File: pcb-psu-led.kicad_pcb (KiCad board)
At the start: 2 copper layers, 140 x 80 mm, 16 parts, among them J1 MKDS 1,5/2-5,08, J2 LED PANEL OUT, T1 Talema 70000K, U1 LM78L05ACZ

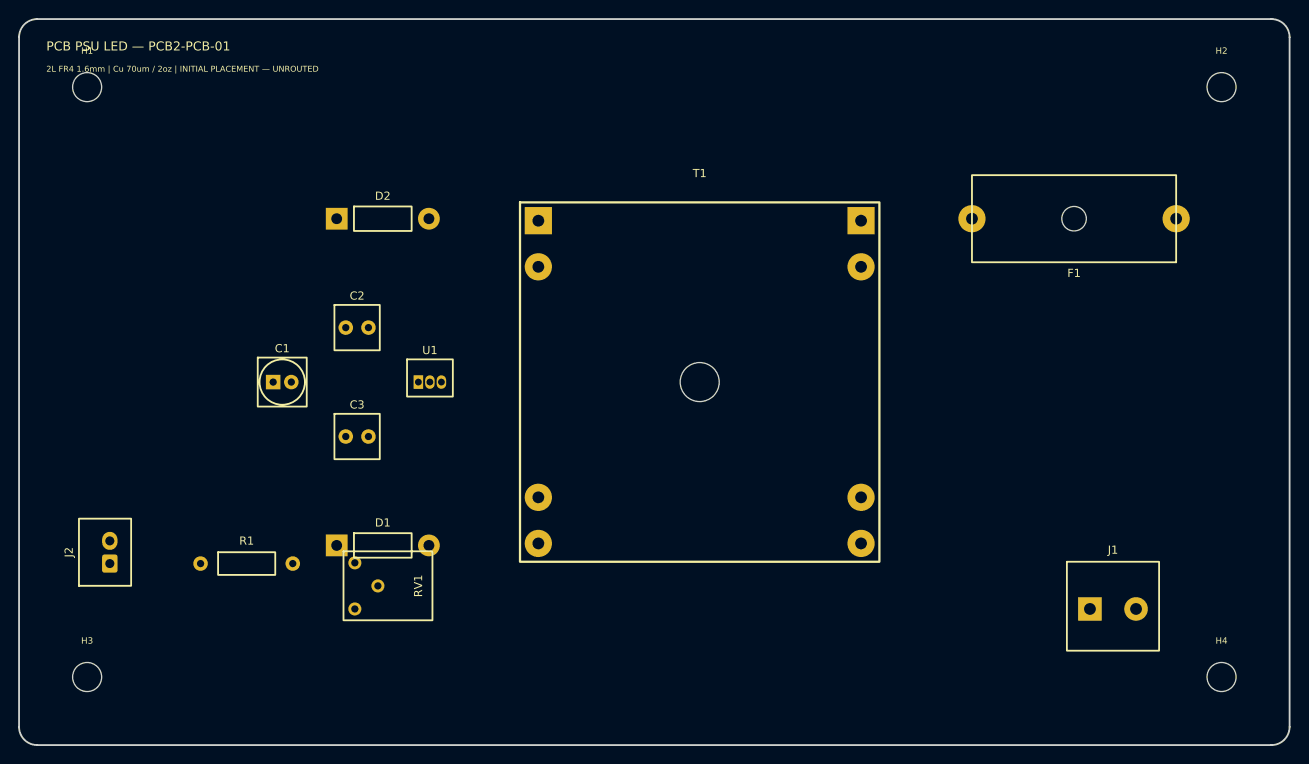
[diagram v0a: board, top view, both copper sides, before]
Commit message: PCB2-PCB-03: route board and segregate mains from SELV
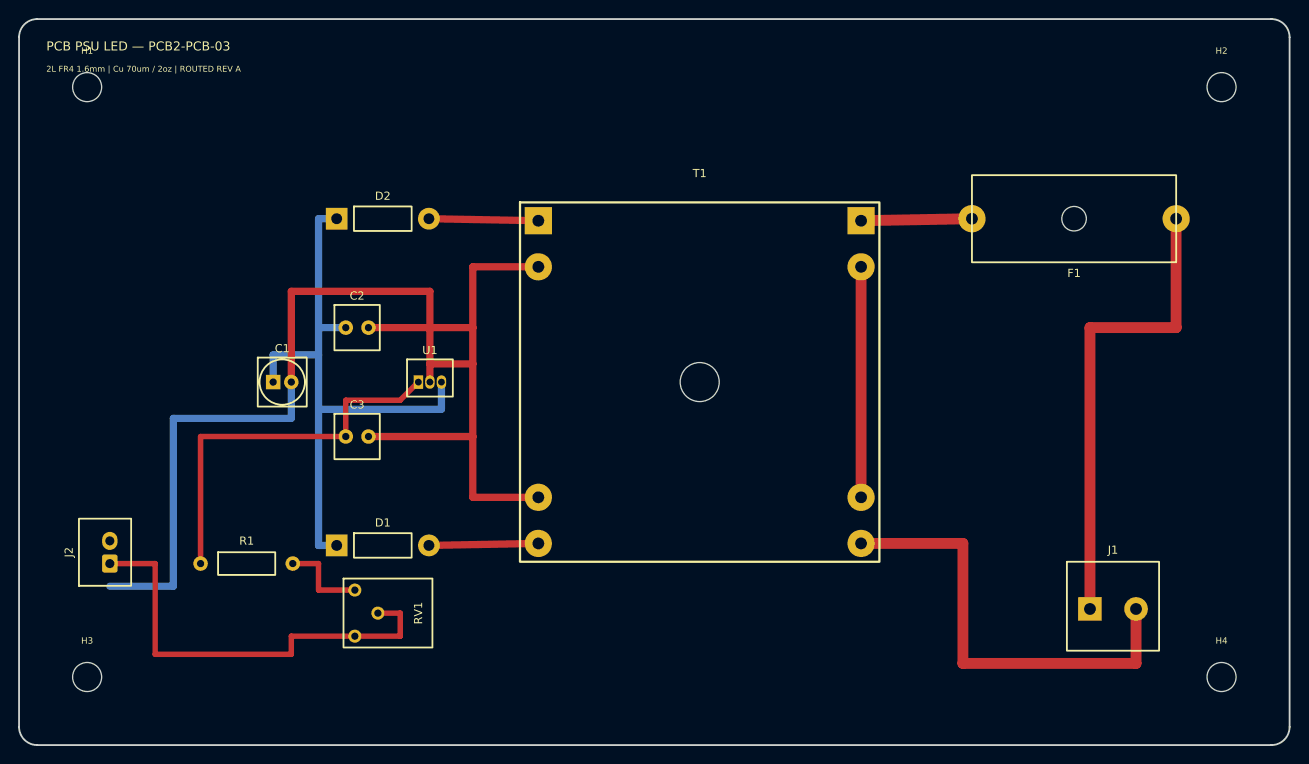
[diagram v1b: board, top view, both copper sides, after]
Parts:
- moved RV1 3.00 mm to (37.0, 68.0)
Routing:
- net CT_RAW: track 0.00 -> 145.3 mm
- net VRAW_PLUS: track 0.00 -> 67.5 mm
- net L_SW: track 0.00 -> 52.5 mm
- net N_SW: track 0.00 -> 49.5 mm
- net LED_ANODE_OUT: track 0.00 -> 49.0 mm
- net PLUS_5V_LED: track 0.00 -> 42.8 mm
- net PRI_LINK_5_4: track 0.00 -> 25.4 mm
- net Net-(F1-Pad2): track 0.00 -> 12.2 mm
- net SEC_B: track 0.00 -> 12.1 mm
- net SEC_A: track 0.00 -> 12.1 mm
- net Net-(R1-Pad2): track 0.00 -> 9.76 mm
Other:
- board text added: "2L FR4 1.6mm | Cu 70um / 2oz | ROUTED REV A"
- board text added: "MAINS ROUTING AREA"
- board text added: "NO EXTERNAL COPPER — TRANSFORMER ISOLATION CORRIDOR"
- board text added: "PCB PSU LED — PCB2-PCB-03"
- board text added: "SELV ROUTING AREA"
- board text removed: "2L FR4 1.6mm | Cu 70um / 2oz | INITIAL PLACEMENT — UNROUTED"
- board text removed: "MAINS AREA"
- board text removed: "PCB PSU LED — PCB2-PCB-01"
- board text removed: "SELV AREA"
- board text removed: "TRANSFORMER ISOLATION BARRIER"
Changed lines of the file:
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@@
     (title "PCB PSU LED")
     (date "2026-07-16")
-    (rev "PCB2-PCB-01")
+    (rev "PCB2-PCB-03")
     (company "Custom Step-Down PSU 230 V to 100 V")
-    (comment 1 "Initial board outline and component placement")
+    (comment 1 "Routed board with mains and SELV segregation")
   )
   (layers
@@
   )
   (footprint "Potentiometer_THT:Potentiometer_Bourns_3386P_Vertical" (layer "F.Cu")
-    (at 37 65 0)
+    (at 37 68 0)
     (attr through_hole)
     (fp_text reference "RV1" (at 7 -2.54 90) (layer "F.SilkS")
@@
     )
   )
+  (segment (start 118 65) (end 118 34) (width 1.2) (layer "F.Cu") (net 1))
+  (segment (start 118 34) (end 127.5 34) (width 1.2) (layer "F.Cu") (net 1))
+  (segment (start 127.5 34) (end 127.5 22) (width 1.2) (layer "F.Cu") (net 1))
+  (segment (start 123.08 65) (end 123.08 71) (width 1.2) (layer "F.Cu") (net 2))
+  (segment (start 123.08 71) (end 104 71) (width 1.2) (layer "F.Cu") (net 2))
+  (segment (start 104 71) (end 104 57.78) (width 1.2) (layer "F.Cu") (net 2))
+  (segment (start 104 57.78) (end 92.78 57.78) (width 1.2) (layer "F.Cu") (net 2))
+  (segment (start 105 22) (end 92.78 22.22) (width 1.2) (layer "F.Cu") (net 10))
+  (segment (start 92.78 27.3) (end 92.78 52.7) (width 1.2) (layer "F.Cu") (net 3))
+  (segment (start 45.16 22) (end 57.22 22.22) (width 0.8) (layer "F.Cu") (net 4))
+  (segment (start 45.16 58) (end 57.22 57.78) (width 0.8) (layer "F.Cu") (net 5))
+  (segment (start 33 22) (end 33 34) (width 0.8) (layer "B.Cu") (net 7))
+  (segment (start 33 34) (end 33 37) (width 0.8) (layer "B.Cu") (net 7))
+  (segment (start 33 37) (end 33 43) (width 0.8) (layer "B.Cu") (net 7))
+  (segment (start 33 43) (end 33 58) (width 0.8) (layer "B.Cu") (net 7))
+  (segment (start 35 22) (end 33 22) (width 0.8) (layer "B.Cu") (net 7))
+  (segment (start 35 58) (end 33 58) (width 0.8) (layer "B.Cu") (net 7))
+  (segment (start 28 40) (end 28 37) (width 0.8) (layer "B.Cu") (net 7))
+  (segment (start 28 37) (end 33 37) (width 0.8) (layer "B.Cu") (net 7))
+  (segment (start 36 34) (end 33 34) (width 0.8) (layer "B.Cu") (net 7))
+  (segment (start 46.54 40) (end 46.54 43) (width 0.8) (layer "B.Cu") (net 7))
+  (segment (start 46.54 43) (end 33 43) (width 0.8) (layer "B.Cu") (net 7))
+  (segment (start 50 27.3) (end 50 34) (width 0.8) (layer "F.Cu") (net 6))
+  (segment (start 50 34) (end 50 38) (width 0.8) (layer "F.Cu") (net 6))
+  (segment (start 50 38) (end 50 46) (width 0.8) (layer "F.Cu") (net 6))
+  (segment (start 50 46) (end 50 52.7) (width 0.8) (layer "F.Cu") (net 6))
+  (segment (start 57.22 27.3) (end 50 27.3) (width 0.8) (layer "F.Cu") (net 6))
+  (segment (start 57.22 52.7) (end 50 52.7) (width 0.8) (layer "F.Cu") (net 6))
+  (segment (start 38.5 34) (end 50 34) (width 0.8) (layer "F.Cu") (net 6))
+  (segment (start 38.5 46) (end 50 46) (width 0.8) (layer "F.Cu") (net 6))
+  (segment (start 45.27 40) (end 45.27 38) (width 0.8) (layer "F.Cu") (net 6))
+  (segment (start 45.27 38) (end 50 38) (width 0.8) (layer "F.Cu") (net 6))
+  (segment (start 30 40) (end 30 30) (width 0.8) (layer "F.Cu") (net 6))
+  (segment (start 30 30) (end 45.27 30) (width 0.8) (layer "F.Cu") (net 6))
+  (segment (start 45.27 30) (end 45.27 38) (width 0.8) (layer "F.Cu") (net 6))
+  (segment (start 30 40) (end 30 44) (width 0.8) (layer "B.Cu") (net 6))
+  (segment (start 30 44) (end 17 44) (width 0.8) (layer "B.Cu") (net 6))
+  (segment (start 17 44) (end 17 62.5) (width 0.8) (layer "B.Cu") (net 6))
+  (segment (start 17 62.5) (end 10 62.5) (width 0.8) (layer "B.Cu") (net 6))
+  (segment (start 44 40) (end 42 42) (width 0.6) (layer "F.Cu") (net 8))
+  (segment (start 42 42) (end 36 42) (width 0.6) (layer "F.Cu") (net 8))
+  (segment (start 36 42) (end 36 46) (width 0.6) (layer "F.Cu") (net 8))
+  (segment (start 36 46) (end 20 46) (width 0.6) (layer "F.Cu") (net 8))
+  (segment (start 20 46) (end 20 60) (width 0.6) (layer "F.Cu") (net 8))
+  (segment (start 30.16 60) (end 33 60) (width 0.6) (layer "F.Cu") (net 11))
+  (segment (start 33 60) (end 33 62.92) (width 0.6) (layer "F.Cu") (net 11))
+  (segment (start 33 62.92) (end 37 62.92) (width 0.6) (layer "F.Cu") (net 11))
+  (segment (start 39.54 65.46) (end 42 65.46) (width 0.6) (layer "F.Cu") (net 9))
+  (segment (start 42 65.46) (end 42 68) (width 0.6) (layer "F.Cu") (net 9))
+  (segment (start 42 68) (end 37 68) (width 0.6) (layer "F.Cu") (net 9))
+  (segment (start 37 68) (end 30 68) (width 0.6) (layer "F.Cu") (net 9))
+  (segment (start 30 68) (end 30 70) (width 0.6) (layer "F.Cu") (net 9))
+  (segment (start 30 70) (end 15 70) (width 0.6) (layer "F.Cu") (net 9))
+  (segment (start 15 70) (end 15 60) (width 0.6) (layer "F.Cu") (net 9))
+  (segment (start 15 60) (end 10 60) (width 0.6) (layer "F.Cu") (net 9))
   (gr_line (start 2 0) (end 138 0) (stroke (width 0.2) (type default)) (layer "Edge.Cuts"))
   (gr_arc (start 138 0) (mid 139.4142 0.5858) (end 140 2) (stroke (width 0.2) (type default)) (layer "Edge.Cuts"))
@@
   (gr_line (start 0 78) (end 0 2) (stroke (width 0.2) (type default)) (layer "Edge.Cuts"))
   (gr_arc (start 0 2) (mid 0.5858 0.5858) (end 2 0) (stroke (width 0.2) (type default)) (layer "Edge.Cuts"))
-  (gr_text "PCB PSU LED — PCB2-PCB-01" (at 3 3) (layer "F.SilkS")
+  (gr_text "PCB PSU LED — PCB2-PCB-03" (at 3 3) (layer "F.SilkS")
     (effects (font (size 1 1) (thickness 0.15)) (justify left))
   )
-  (gr_text "2L FR4 1.6mm | Cu 70um / 2oz | INITIAL PLACEMENT — UNROUTED" (at 3 5.5) (layer "F.SilkS")
+  (gr_text "2L FR4 1.6mm | Cu 70um / 2oz | ROUTED REV A" (at 3 5.5) (layer "F.SilkS")
     (effects (font (size 0.65 0.65) (thickness 0.12)) (justify left))
   )
-  (gr_line (start 50 8) (end 50 72) (stroke (width 0.3) (type dash)) (layer "Dwgs.User"))
-  (gr_text "SELV AREA" (at 25 8) (layer "Dwgs.User")
+  (gr_line (start 62 8) (end 62 72) (stroke (width 0.3) (type dash)) (layer "Dwgs.User"))
+  (gr_line (start 88 8) (end 88 72) (stroke (width 0.3) (type dash)) (layer "Dwgs.User"))
+  (gr_text "SELV ROUTING AREA" (at 25 8) (layer "Dwgs.User")
     (effects (font (size 0.8 0.8) (thickness 0.12)))
   )
-  (gr_text "TRANSFORMER ISOLATION BARRIER" (at 75 72) (layer "Dwgs.User")
+  (gr_text "NO EXTERNAL COPPER — TRANSFORMER ISOLATION CORRIDOR" (at 75 72) (layer "Dwgs.User")
     (effects (font (size 0.75 0.75) (thickness 0.12)))
   )
-  (gr_text "MAINS AREA" (at 116 8) (layer "Dwgs.User")
+  (gr_text "MAINS ROUTING AREA" (at 116 8) (layer "Dwgs.User")
     (effects (font (size 0.8 0.8) (thickness 0.12)))
   )

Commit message: PCB2-PCB-03R1: synchronize board with schematic
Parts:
- removed H1, H2, H3, H4: M3 NPTH, MountingHole:MountingHole_3.2mm_M3
- C1: value 47uF 25V -> 47uF 25V Panasonic FR
- J1: value MKDS 1,5/2-5,08 -> MAINS INPUT 230V
- J2: value LED PANEL OUT -> LED PANEL OUT JST XH
- RV1: value 5k 3386P -> 5k Bourns 3386P
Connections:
- net CT_RAW renamed /CT_RAW
- net LED_ANODE_OUT renamed /LED_ANODE_OUT
- net L_SW renamed /L_SW
- net N_SW renamed /N_SW
- net PLUS_5V_LED renamed /PLUS_5V_LED
- net PRI_LINK_5_4 renamed /PRI_LINK_5_4
- net SEC_A renamed /SEC_A
- net SEC_B renamed /SEC_B
- net VRAW_PLUS renamed /VRAW_PLUS
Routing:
- net /CT_RAW: track 145.3 -> 150.3 mm
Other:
- outline, holes or cut-outs redrawn

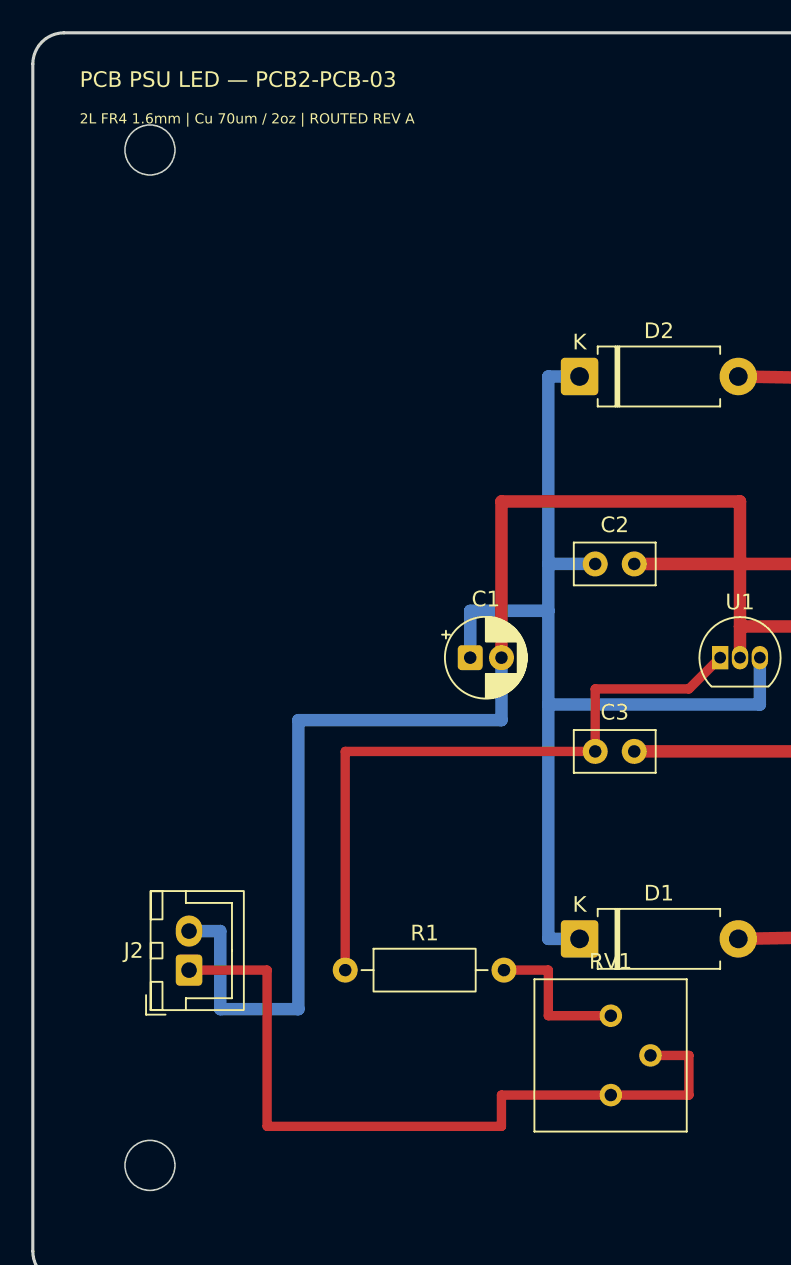
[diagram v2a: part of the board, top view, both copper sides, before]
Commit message: PCB2-PCB-03R2: clean DRC footprint and silkscreen warnings
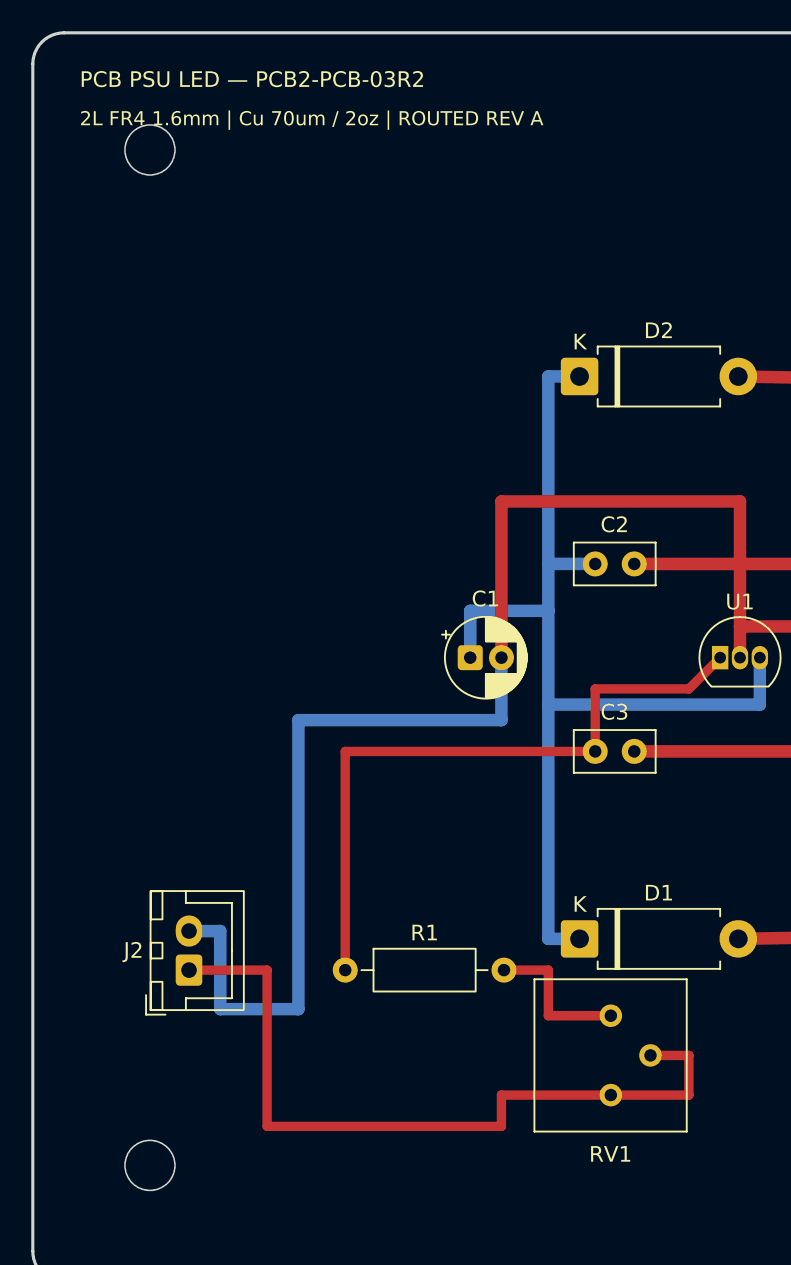
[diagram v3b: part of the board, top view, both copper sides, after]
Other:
- board text added: "PCB PSU LED — PCB2-PCB-03R2"
- board text removed: "PCB PSU LED — PCB2-PCB-03"

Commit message: PCB2-PCB-03R3: apply frozen footprints and clean DRC
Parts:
- F1: footprint Fuse:Fuseholder_Cylinder-5x20mm_Schurter_0031_8201_Horizontal_Open -> PSU_LED:Fuseholder_Cylinder-5x20mm_Schurter_0031_8201_Horizontal_Open
- J2: footprint Connector_JST:JST_XH_B2B-XH-A_1x02_P2.50mm_Vertical -> PSU_LED:JST_XH_B2B-XH-A_1x02_P2.50mm_Vertical
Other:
- board text added: "2L FR4 1.6mm | Cu 70um / 2oz | PCB2-PCB-03R3"
- board text added: "PCB PSU LED — PCB2-PCB-03R3"
- board text removed: "2L FR4 1.6mm | Cu 70um / 2oz | ROUTED REV A"
- board text removed: "PCB PSU LED — PCB2-PCB-03R2"
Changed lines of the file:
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@@
     (title "PCB PSU LED")
     (date "2026-07-16")
-    (rev "PCB2-PCB-03R2")
+    (rev "PCB2-PCB-03R3")
     (company "Custom Step-Down PSU 230 V to 100 V")
     (comment 1 "Schematic-synchronized routed board")
@@
   	)
   )
-  (footprint "Fuse:Fuseholder_Cylinder-5x20mm_Schurter_0031_8201_Horizontal_Open"
+  (footprint "PSU_LED:Fuseholder_Cylinder-5x20mm_Schurter_0031_8201_Horizontal_Open"
     (layer "F.Cu")
     (at 127.5 22 180)
@@
   	)
   )
-  (footprint "Connector_JST:JST_XH_B2B-XH-A_1x02_P2.50mm_Vertical"
+  (footprint "PSU_LED:JST_XH_B2B-XH-A_1x02_P2.50mm_Vertical"
     (layer "F.Cu")
     (at 10 60 90)
@@
   (gr_line (start 0 78) (end 0 2) (stroke (width 0.2) (type default)) (layer "Edge.Cuts"))
   (gr_arc (start 0 2) (mid 0.5858 0.5858) (end 2 0) (stroke (width 0.2) (type default)) (layer "Edge.Cuts"))
-  (gr_text "PCB PSU LED — PCB2-PCB-03R2" (at 3 3) (layer "F.SilkS")
+  (gr_text "PCB PSU LED — PCB2-PCB-03R3" (at 3 3) (layer "F.SilkS")
     (effects (font (size 1 1) (thickness 0.15)) (justify left))
   )
-  (gr_text "2L FR4 1.6mm | Cu 70um / 2oz | ROUTED REV A" (at 3 5.5) (layer "F.SilkS")
+  (gr_text "2L FR4 1.6mm | Cu 70um / 2oz | PCB2-PCB-03R3" (at 20 5.5) (layer "F.SilkS")
     (effects (font (size 0.9 0.9) (thickness 0.12)) (justify left))
   )

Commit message: PCB2-PCB-04: add NPTH mounting holes and 6 mm safety rule
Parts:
- added H1: MountingHole_3.2mm_M3, MountingHole_3.2mm_M3, F.Cu at (7.50, 7.50)
- added H2: MountingHole_3.2mm_M3, MountingHole_3.2mm_M3, F.Cu at (132.5, 7.50)
- added H3: MountingHole_3.2mm_M3, MountingHole_3.2mm_M3, F.Cu at (7.50, 72.5)
- added H4: MountingHole_3.2mm_M3, MountingHole_3.2mm_M3, F.Cu at (132.5, 72.5)
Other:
- outline, holes or cut-outs redrawn

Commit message: PCB2-PCB-04R1: add production connector markings
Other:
- board text added: "0V"
- board text added: "2L FR4 1.6mm | Cu 70um / 2oz | PCB2-PCB-04R1"
- board text added: "L"
- board text added: "LED+"
- board text added: "N"
- board text added: "PCB PSU LED — PCB2-PCB-04R1"
- board text removed: "2L FR4 1.6mm | Cu 70um / 2oz | PCB2-PCB-03R3"
- board text removed: "PCB PSU LED — PCB2-PCB-03R3"
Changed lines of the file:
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@@
     (title "PCB PSU LED")
     (date "2026-07-16")
-    (rev "PCB2-PCB-04")
+    (rev "PCB2-PCB-04R1")
     (company "Custom Step-Down PSU 230 V to 100 V")
-    (comment 1 "Production DFM: NPTH M3 holes, copper keepouts, 6 mm MAINS-SELV rule")
+    (comment 1 "Production marking review: connector polarity and revision identification")
   )
   (layers
@@
   (gr_line (start 0 78) (end 0 2) (stroke (width 0.2) (type default)) (layer "Edge.Cuts"))
   (gr_arc (start 0 2) (mid 0.5858 0.5858) (end 2 0) (stroke (width 0.2) (type default)) (layer "Edge.Cuts"))
-  (gr_text "PCB PSU LED — PCB2-PCB-03R3" (at 3 3) (layer "F.SilkS")
+  (gr_text "PCB PSU LED — PCB2-PCB-04R1" (at 3 3) (layer "F.SilkS")
     (effects (font (size 1 1) (thickness 0.15)) (justify left))
   )
-  (gr_text "2L FR4 1.6mm | Cu 70um / 2oz | PCB2-PCB-03R3" (at 20 5.5) (layer "F.SilkS")
+  (gr_text "2L FR4 1.6mm | Cu 70um / 2oz | PCB2-PCB-04R1" (at 20 5.5) (layer "F.SilkS")
     (effects (font (size 0.9 0.9) (thickness 0.12)) (justify left))
   )
@@
     (effects (font (size 0.8 0.8) (thickness 0.12)))
   )
+  (gr_text "L" (at 118 68.5) (layer "F.SilkS")
+    (effects (font (size 1 1) (thickness 0.15)))
+  )
+  (gr_text "N" (at 123.08 68.5) (layer "F.SilkS")
+    (effects (font (size 1 1) (thickness 0.15)))
+  )
+  (gr_text "LED+" (at 6.5 60) (layer "F.SilkS")
+    (effects (font (size 0.8 0.8) (thickness 0.12)) (justify right))
+  )
+  (gr_text "0V" (at 6.5 62.5) (layer "F.SilkS")
+    (effects (font (size 0.8 0.8) (thickness 0.12)) (justify right))
+  )
   (embedded_fonts no)
